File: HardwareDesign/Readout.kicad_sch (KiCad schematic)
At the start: 12 parts, among them U701 74ACT163, U702 74ACT163, U703 74ACT163, U705 74ACT273, U706 74ACT273, U707 GAL22V10

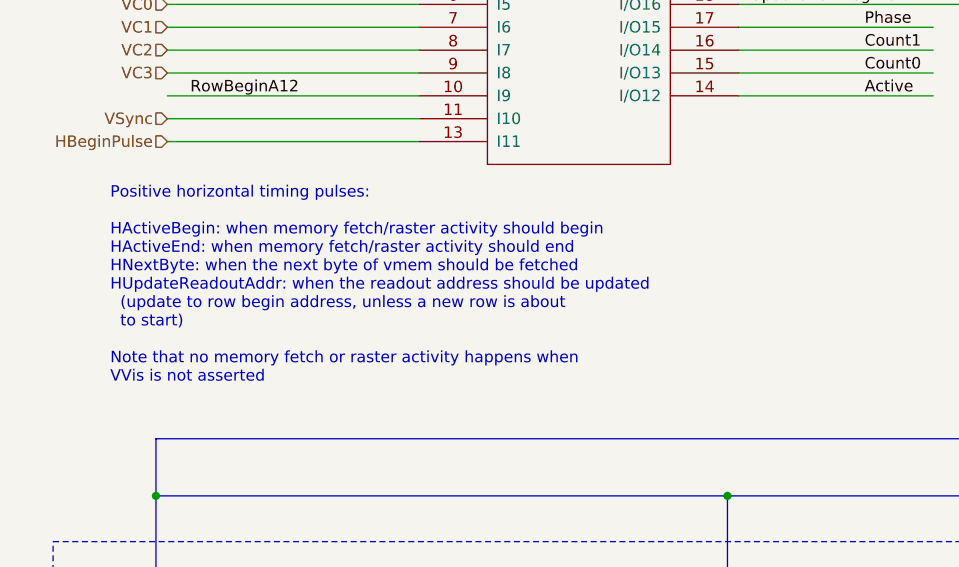
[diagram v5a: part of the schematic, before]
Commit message: remove explanatory text about horizontal timing
ROutCtrl.pld is a more authoritative source of information
about horizontal timing (and of course the simulation
as well.)
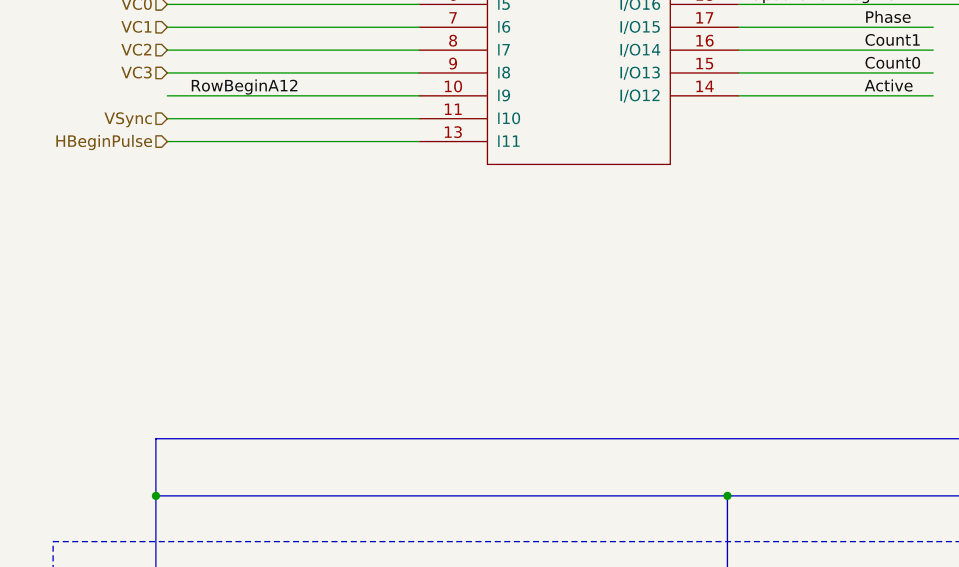
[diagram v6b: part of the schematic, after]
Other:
- note removed: "Positive horizontal timing pulses: HActiveBegin: when memory fetch/raster activity should begin HActiveEnd: when memory fetch/raster activity should end HNextByte: when the next byte of vmem should be fetched HUpdateReadoutAddr: when the readout address should be updated (update to row begin address, unless a new row is about to start) Note that no memory fetch or raster activity happens when VVi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"
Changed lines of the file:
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@@
-		)
-	)
-	(text "Positive horizontal timing pulses:\n\nHActiveBegin: when memory fetch/raster activity should begin\nHActiveEnd: when memory fetch/raster activity should end\nHNextByte: when the next byte of vmem should be fetched\nHUpdateReadoutAddr: when the readout address should be updated\n  (update to row begin address, unless a new row is about\n  to start)\n\nNote that no memory fetch or raster activity happens when\nVVis is not asserted"
-		(exclude_from_sim no)
-		(at 26.67 88.392 0)
-		(effects
-			(font
-				(size 1.27 1.27)
-			)
-			(justify left)
 		)
 	)

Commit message: mention which file has logic for readout ctrl GAL
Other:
- note added: "Logic is defined in ROutCtrl.pld"
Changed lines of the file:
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@@
+		)
+	)
+	(text "Logic is defined in\nROutCtrl.pld"
+		(exclude_from_sim no)
+		(at 79.248 24.13 0)
+		(effects
+			(font
+				(size 1.27 1.27)
+			)
 		)
 	)
